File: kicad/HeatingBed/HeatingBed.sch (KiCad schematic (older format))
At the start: 32 parts, among them J1 Conn_01x08_Female, J2 Conn_01x08_Male, J3 Conn_01x02_Female, J4 Conn_01x02_Male, J5 Conn_01x02, J6 Conn_01x02, K1 EC2-3NU, Q1 BC182, T1 Trasf 220V-9,5V, U1 I2c_LCD, U2 MOC3032M, U3 78L05

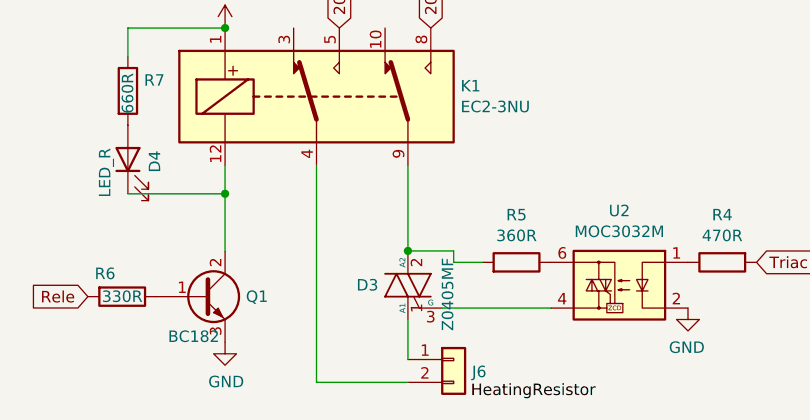
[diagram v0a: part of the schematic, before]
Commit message: Update SCR on schematical
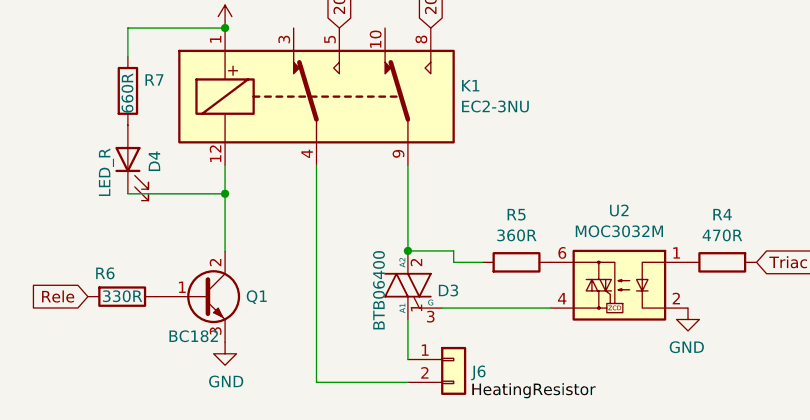
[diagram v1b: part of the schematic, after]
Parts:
- D3: value Z0405MF -> BTB06400
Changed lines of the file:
@@
 U 1 1 61FAA17E
 P 8800 5475
-F 0 "D3" H 8929 5475 50  0000 L CNN
-F 1 "Z0405MF" V 8625 5275 50  0000 L CNN
+F 0 "D3" H 8575 5450 50  0000 L CNN
+F 1 "BTB06400" V 8925 5275 50  0000 L CNN
 F 2 "" V 8875 5500 50  0001 C CNN
 F 3 "~" V 8800 5475 50  0001 C CNN
